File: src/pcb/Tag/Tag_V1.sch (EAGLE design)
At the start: 28 parts, among them IC1 ATMEGA328P-AU, IC2 DWM1000, IC3 MIC5219-3.3YM5-TR, J1 AVR_SPI_PROG_3X2PTH, Q1 8MHz

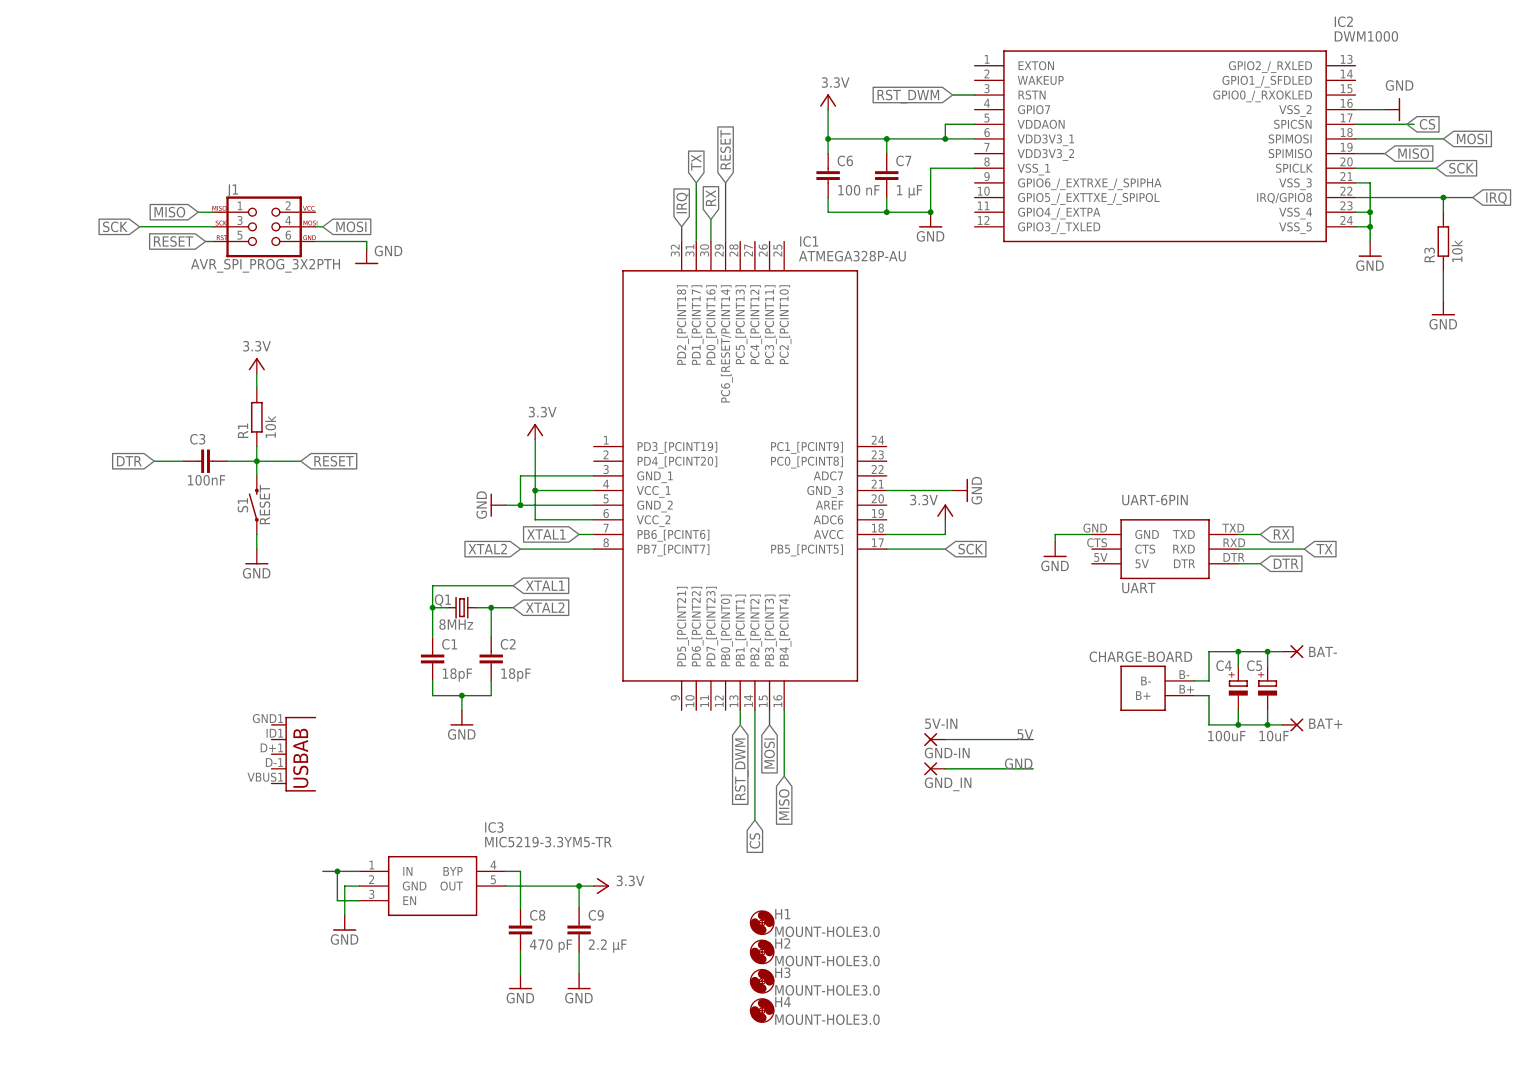
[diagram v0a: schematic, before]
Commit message: Final version V1 tag
-Uses MIC5219 to convert 5V to 3.3V
-DWM module is now soldered on the PCB
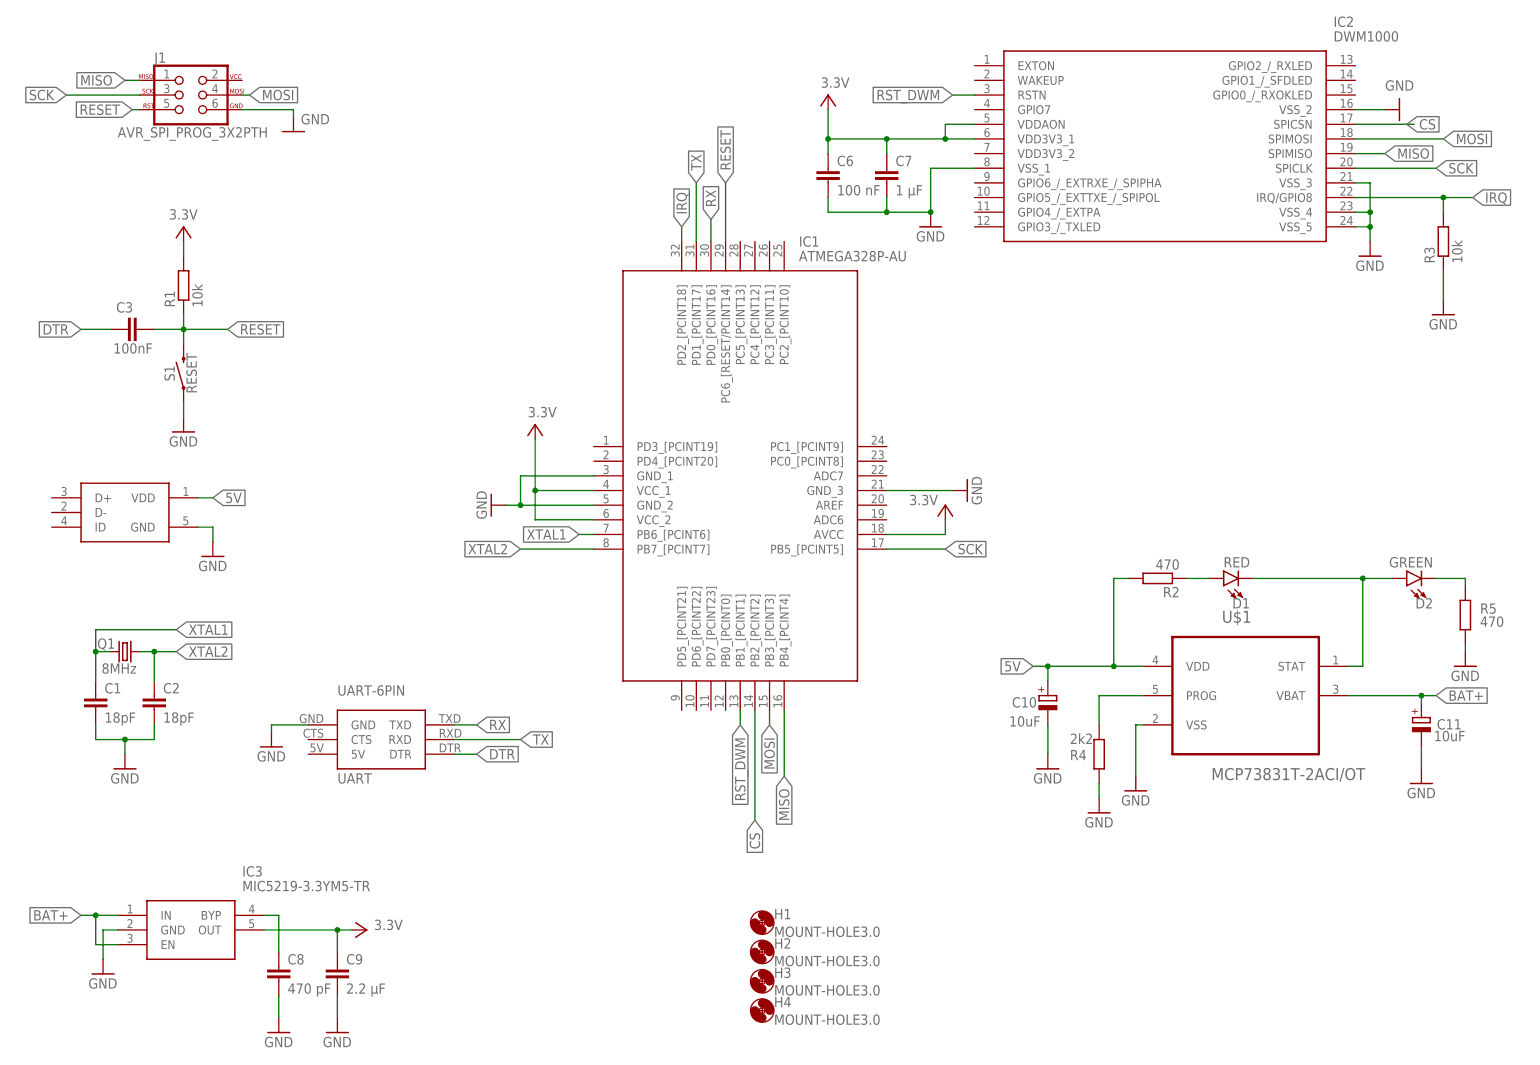
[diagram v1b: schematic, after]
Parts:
- removed 5V-IN, BAT+, BAT-: (no value), wirepad:2,15/1,0
- removed C4: 100uF, rcl:CPOL-EUE3.5-8
- removed C5: 10uF, rcl:CPOL-EUE2.5-7
- removed GND-IN: GND_IN, wirepad:2,15/1,0
- removed U$4: 18650-CHARGE-5V-OUT, Eigen Library:18650-CHARGE-5V-OUT
- added C10, C11: 10uF, rcl:CPOL-EUE2.5-7
- added D1: RED, SparkFun-LED:LED-RED1206
- added D2: GREEN, SparkFun-LED:LED-GREEN1206
- added R2, R5: 470, rcl:R-EU_R0805
- added R4: 2k2, rcl:R-EU_R0805
- added U$1: MCP73831T-2ACI/OT, MCP73831T-2ACI_OT:MCP73831T-2ACI/OT
- U1: value (none) -> 105017-0001; device MicroUSB:USB"" -> 105017-0001:105017-0001
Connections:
- new net BAT+: C11.+, IC3.EN, IC3.IN, U$1.VBAT
- new net N$6: R4.1, U$1.PROG
- net 5V: now also C10.+, R2.2, U$1.VDD, U1.VDD; no longer 5V-IN.P
- net GND: now also C10.-, C11.-, R4.2, R5.2, U$1.VSS, U1.GND; no longer GND-IN.P
- net N$1: now also D1.C, D2.A, U$1.STAT; no longer BAT-.P, C4.+, C5.+, U$4.B-
- net N$2: now also D1.A, R2.1; no longer BAT+.P, C4.-, C5.-, U$4.B+
- net N$4: now also D2.C, R5.1; no longer IC3.EN, IC3.IN
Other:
- note removed: "CHARGE-BOARD"
- moved on the sheet: C1, C2, C3, C8, C9, IC3, J1, Q1, R1, S1

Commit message: Versie 2 tag batterijen op PCB
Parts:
- added BT1, BT2: (no value), SparkFun-Batteries:BATTERY-18650
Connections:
- net BAT+: now also BT1.+, BT2.+
- net GND: now also BT1.-, BT2.-
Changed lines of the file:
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@@
 <part name="GND18" library="supply1" library_urn="urn:adsk.eagle:library:371" deviceset="GND" device=""/>
 <part name="R5" library="rcl" library_urn="urn:adsk.eagle:library:334" deviceset="R-EU_" device="R0805" package3d_urn="urn:adsk.eagle:package:23553/2" value="470"/>
+<part name="BT1" library="SparkFun-Batteries" deviceset="BATTERY" device="-18650"/>
+<part name="BT2" library="SparkFun-Batteries" deviceset="BATTERY" device="-18650"/>
+<part name="GND19" library="supply1" library_urn="urn:adsk.eagle:library:371" deviceset="GND" device=""/>
+<part name="GND20" library="supply1" library_urn="urn:adsk.eagle:library:371" deviceset="GND" device=""/>
 </parts>
 <sheets>
@@
 <attribute name="NAME" x="255.27" y="80.2386" size="1.778" layer="95"/>
 <attribute name="VALUE" x="255.27" y="77.978" size="1.778" layer="96"/>
+</instance>
+<instance part="BT1" gate="G$1" x="86.36" y="27.94" smashed="yes" rot="R270">
+<attribute name="NAME" x="90.678" y="27.94" size="1.778" layer="95" font="vector" rot="R270" align="bottom-center"/>
+<attribute name="VALUE" x="82.042" y="27.94" size="1.778" layer="96" font="vector" rot="R270" align="top-center"/>
+</instance>
+<instance part="BT2" gate="G$1" x="100.33" y="27.94" smashed="yes" rot="R270">
+<attribute name="NAME" x="104.648" y="27.94" size="1.778" layer="95" font="vector" rot="R270" align="bottom-center"/>
+<attribute name="VALUE" x="96.012" y="27.94" size="1.778" layer="96" font="vector" rot="R270" align="top-center"/>
+</instance>
+<instance part="GND19" gate="1" x="86.36" y="15.24" smashed="yes">
+<attribute name="VALUE" x="83.82" y="12.7" size="1.778" layer="96"/>
+</instance>
+<instance part="GND20" gate="1" x="100.33" y="15.24" smashed="yes">
+<attribute name="VALUE" x="97.79" y="12.7" size="1.778" layer="96"/>
 </instance>
 </instances>
@@
 <pinref part="GND18" gate="1" pin="GND"/>
 <wire x1="252.73" y1="74.93" x2="252.73" y2="73.66" width="0.1524" layer="91"/>
+</segment>
+<segment>
+<pinref part="GND19" gate="1" pin="GND"/>
+<pinref part="BT1" gate="G$1" pin="-"/>
+<wire x1="86.36" y1="17.78" x2="86.36" y2="22.86" width="0.1524" layer="91"/>
+</segment>
+<segment>
+<pinref part="BT2" gate="G$1" pin="-"/>
+<pinref part="GND20" gate="1" pin="GND"/>
+<wire x1="100.33" y1="22.86" x2="100.33" y2="17.78" width="0.1524" layer="91"/>
 </segment>
 </net>
@@
 <label x="247.65" y="66.04" size="1.778" layer="95" xref="yes"/>
 </segment>
-</net>
+<segment>
+<pinref part="BT1" gate="G$1" pin="+"/>
+<wire x1="86.36" y1="33.02" x2="86.36" y2="40.64" width="0.1524" layer="91"/>
+<pinref part="BT2" gate="G$1" pin="+"/>
+<wire x1="86.36" y1="40.64" x2="100.33" y2="40.64" width="0.1524" layer="91"/>
+<wire x1="100.33" y1="40.64" x2="100.33" y2="33.02" width="0.1524" layer="91"/>
+<wire x1="86.36" y1="40.64" x2="81.28" y2="40.64" width="0.1524" layer="91"/>
+<junction x="86.36" y="40.64"/>
+<label x="81.28" y="40.64" size="1.778" layer="95" rot="R180" xref="yes"/>
+</segment>
+</net>
